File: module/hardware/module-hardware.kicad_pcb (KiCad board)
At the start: 4 copper layers, 45.7 x 102.9 mm, 75 parts, among them J1 USB_B_Micro, J10 Conn_01x03, J11 Conn_01x03, J12 Conn_01x03, J2 40Pin 0.1", J3 Conn_01x02_Male, J4 40Pin 0.1", J5 Conn_01x03_Male, J6 Conn_01x03_Male, J7 Conn_01x03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

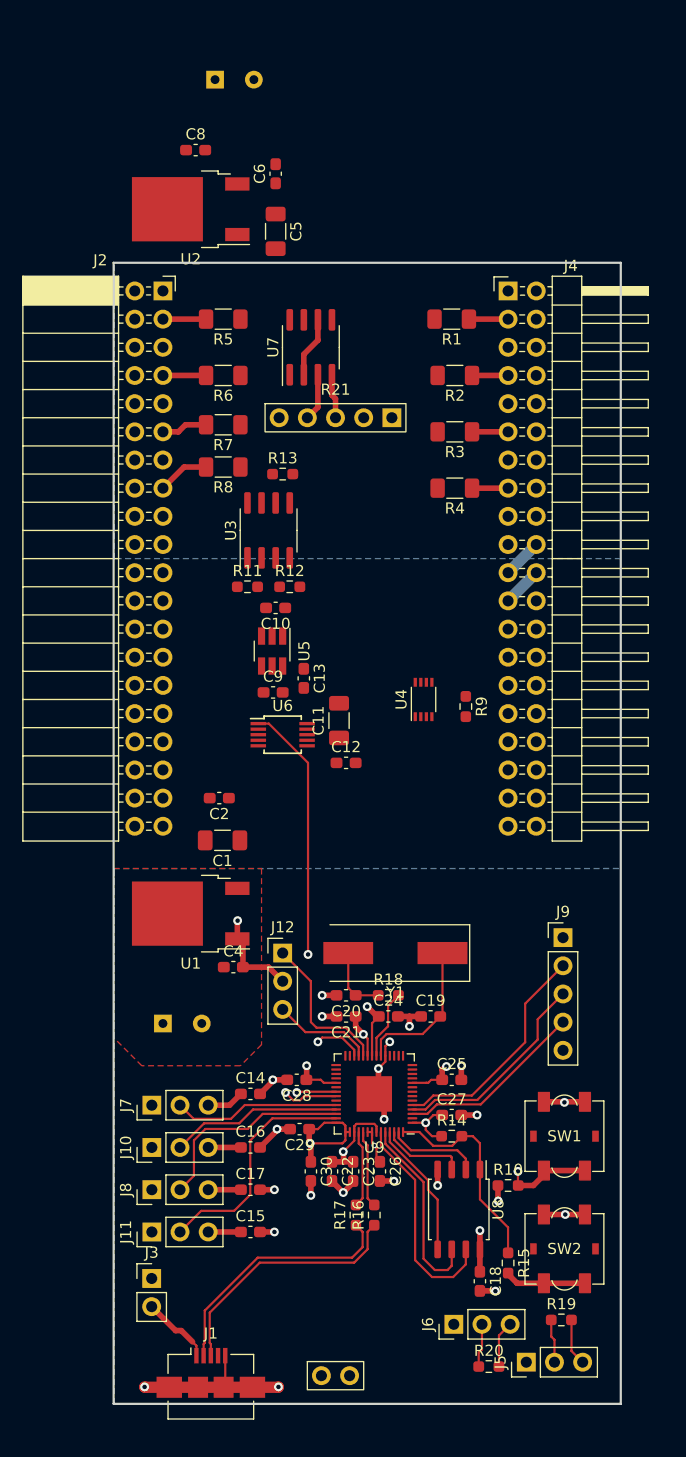
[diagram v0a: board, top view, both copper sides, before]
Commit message: Module Analog preliminaty routing complete
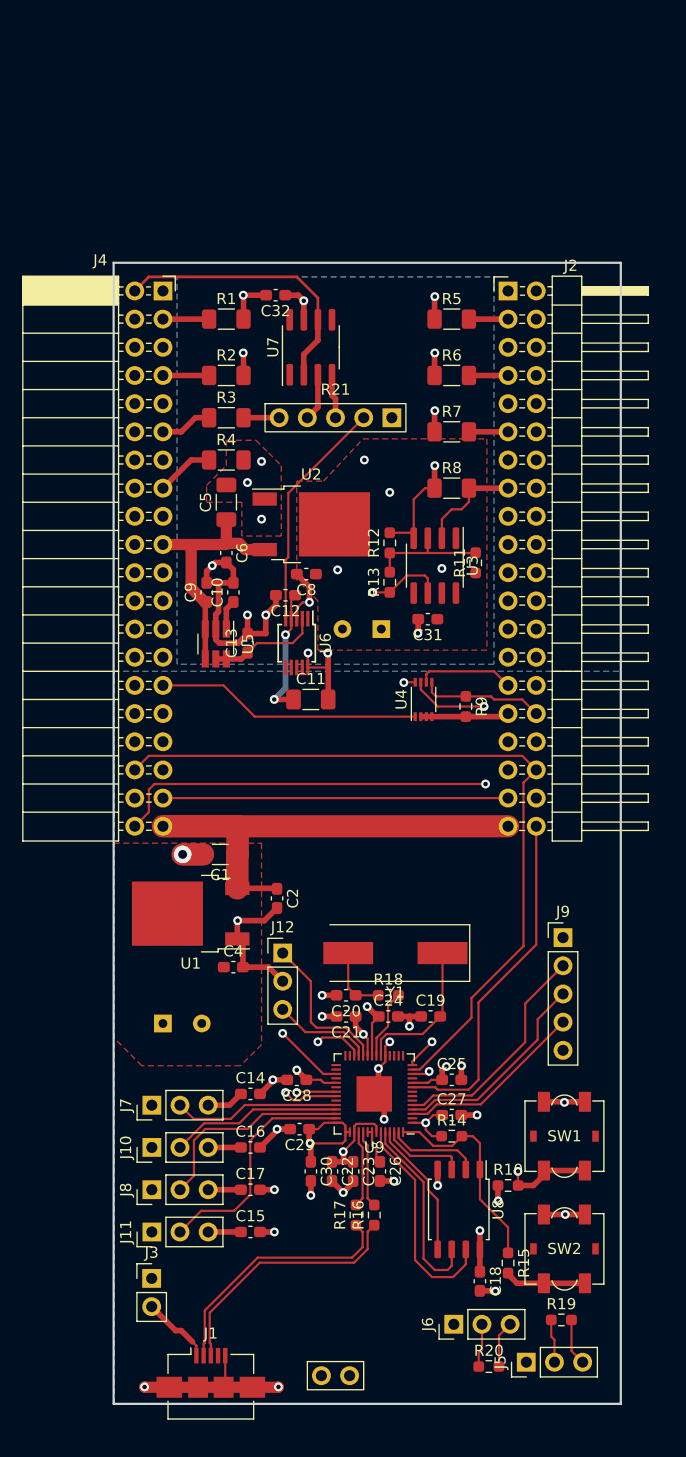
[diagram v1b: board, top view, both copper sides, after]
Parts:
- added C31: 0.1u, Capacitor_SMD:C_0603_1608Metric_Pad1.08x0.95mm_HandSolder, F.Cu at (151.5, 96.9)
- added C32: 0.1u, Capacitor_SMD:C_0603_1608Metric_Pad1.08x0.95mm_HandSolder, F.Cu at (137.8, 67.7)
- J2: footprint Connector_PinSocket_2.54mm:PinSocket_2x20_P2.54mm_Horizontal -> Connector_PinHeader_2.54mm:PinHeader_2x20_P2.54mm_Horizontal
- J4: footprint Connector_PinHeader_2.54mm:PinHeader_2x20_P2.54mm_Horizontal -> Connector_PinSocket_2.54mm:PinSocket_2x20_P2.54mm_Horizontal
- moved C7 51.7 mm to (147.3, 97.8), turned to 180 degrees
- moved C8 39.5 mm to (140.6, 92.8), turned to 180 degrees
- moved C6 34.5 mm to (133.3, 90.9), turned to -90 degrees
- moved J2 31.1 mm to (158.8, 67.3)
- moved J4 31.1 mm to (127.6, 67.3)
- moved U2 30.4 mm to (141.0, 88.4), turned to 0 degrees
- moved C5 24.8 mm to (133.3, 86.4), turned to 90 degrees
- moved R4 20.8 mm to (133.3, 82.5), turned to 0 degrees
- moved R8 20.7 mm to (153.7, 85.1), turned to 0 degrees
- moved R11 20.7 mm to (155.8, 91.8), turned to 90 degrees
- moved R3 20.6 mm to (133.3, 78.7), turned to 0 degrees
- moved R7 20.6 mm to (153.7, 80.0), turned to 0 degrees
- moved R2 20.6 mm to (133.3, 74.9), turned to 0 degrees
- moved R5 20.6 mm to (153.7, 69.8), turned to 0 degrees
- moved R6 20.6 mm to (153.7, 74.9), turned to 0 degrees
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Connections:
- C11 pad 2: GND -> GNDA
- C12 pad 2: GND -> GNDA
- U6 pad 4: (no net) -> +3V3
- U6 pad 7: +3V3 -> /DAC_LDACB
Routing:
- net /CBUS_EXTRA: track 0.00 -> 73.1 mm, vias 0 -> 1
- net /CBUS_SCK: track 0.00 -> 69.3 mm
- net GNDA: track 7.60 -> 74.5 mm, vias 0 -> 16
- net +5VA: track 0.00 -> 60.9 mm
- net /CBUS_DRDY: track 0.00 -> 60.3 mm, vias 0 -> 1
- net /CHANNEL_FULL: track 0.00 -> 57.9 mm, vias 0 -> 2
- net +5VD: track 0.00 -> 48.4 mm
- net /CBUS_SDOUT: track 0.00 -> 43.8 mm, vias 0 -> 2
- net /A7: track 3.25 -> 39.9 mm
- net /A5: track 3.25 -> 39.4 mm
- net /A3: track 3.25 -> 38.9 mm
- net /A1: track 3.53 -> 38.9 mm
- net /A2: track 3.89 -> 38.2 mm
- net /A4: track 3.89 -> 38.2 mm
- net /A6: track 4.15 -> 38.2 mm
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- added copper zone on B.Cu, net +3.3VA
- added copper zone on F.Cu, net +3.3VA
- added copper zone on In2.Cu, net +5VD
- added copper zone on F.Cu, net GNDA
- added copper zone on In1.Cu, net GNDA
- removed copper zone on B.Cu, net GNDA

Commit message: Finish Module PCB routing (DAC SPI lines)
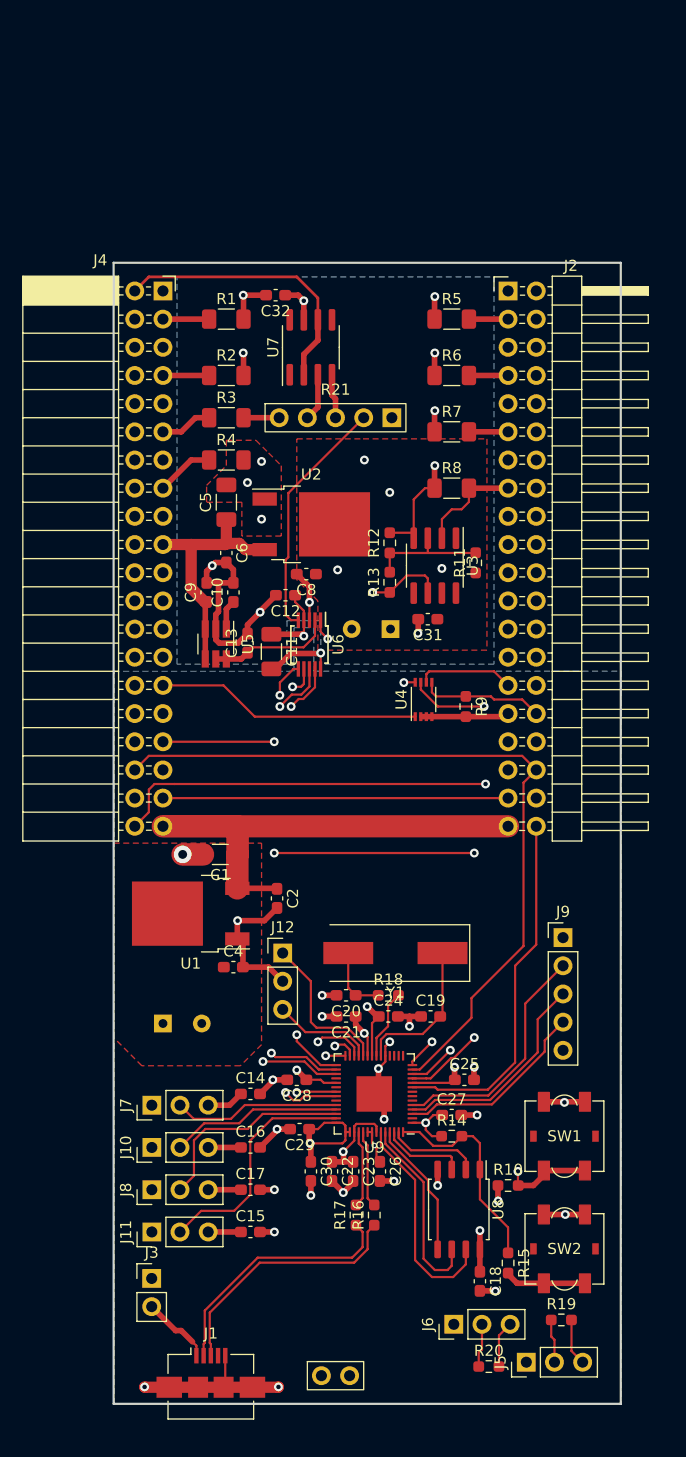
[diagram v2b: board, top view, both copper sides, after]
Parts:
- moved C11 5.59 mm to (137.4, 99.8), turned to -90 degrees
- moved U6 1.15 mm to (140.8, 99.2)
- moved C25 1.14 mm to (154.8, 138.4)
- moved C7 0.83 mm to (148.2, 97.8)
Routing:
- net /CBUS_SDIN: track 0.00 -> 61.8 mm, vias 0 -> 4
- net /DAC_SDAT: track 0.00 -> 43.3 mm, vias 0 -> 2
- net /RUN: track 41.8 -> 84.7 mm, vias 2 -> 3
- net /DAC_CSB: track 0.00 -> 39.9 mm, vias 0 -> 2
- net /DAC_SCK: track 0.00 -> 39.1 mm, vias 0 -> 2
- net /DAC_LDACB: track 0.00 -> 38.6 mm, vias 0 -> 2
- net /CHANNEL_FULL: track 57.9 -> 64.2 mm
- net GNDA: track 74.5 -> 70.3 mm, vias 16 -> 14
- net +3V3: track 72.8 -> 68.7 mm, vias 11 -> 10
- net Net-(C13-Pad1): track 10.1 -> 11.2 mm
- net /CBUS_EXTRA: track 73.1 -> 74.1 mm
- net Net-(R21-Pad2): track 21.0 -> 22.0 mm
- net /D.R.U.M. Module Digital/GPIO3_ENC2: track 20.8 -> 21.7 mm
- net /D.R.U.M. Module Digital/GPIO2_ENC1: track 19.0 -> 19.6 mm
- net /D.R.U.M. Module Digital/GPIO1_ENC0: track 17.0 -> 17.6 mm

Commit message: Fix +5V plane, cleanup silkscreen
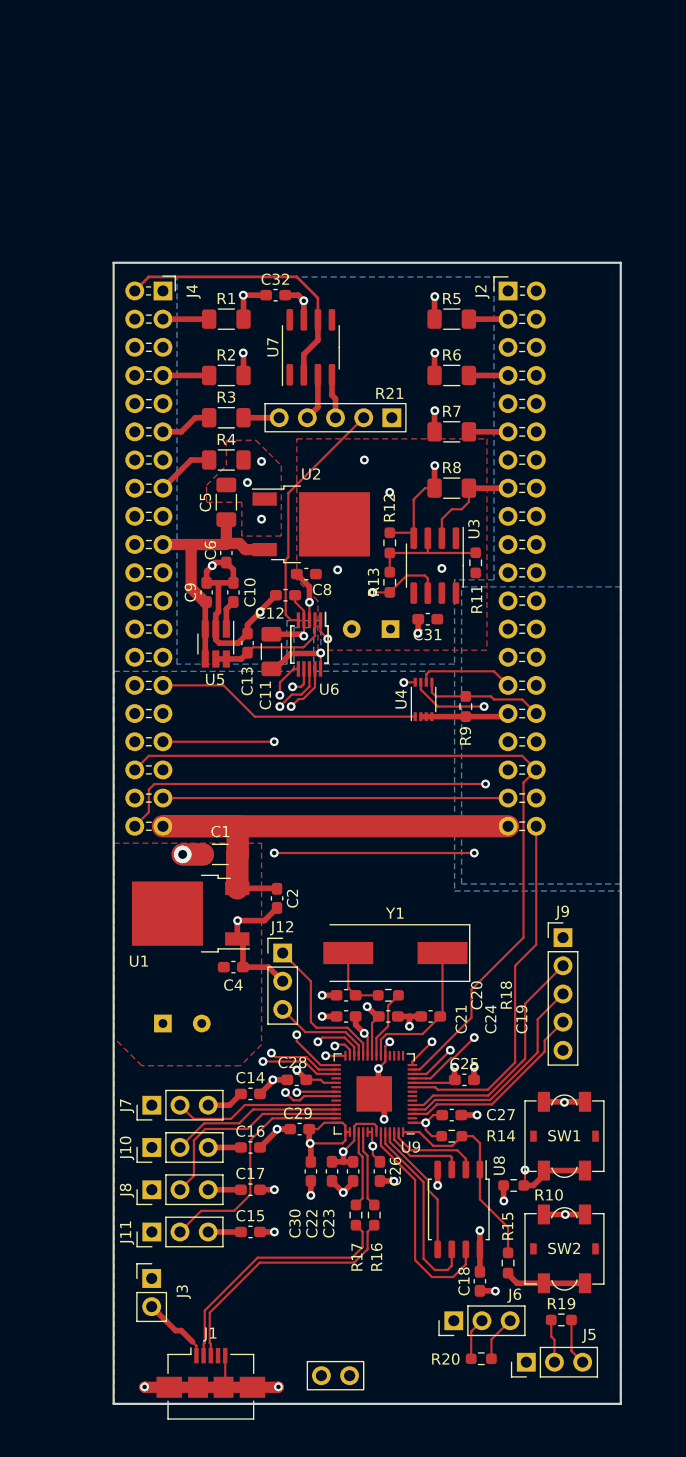
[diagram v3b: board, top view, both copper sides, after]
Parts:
- moved R20 0.98 mm to (156.3, 163.6)
- moved R10 0.51 mm to (159.3, 148.0)
- moved J6 0.32 mm to (153.9, 160.1)
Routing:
- added copper zone on B.Cu, net +5VD

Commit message: John Gibbons 30Khz LP & DAC analog power jumper
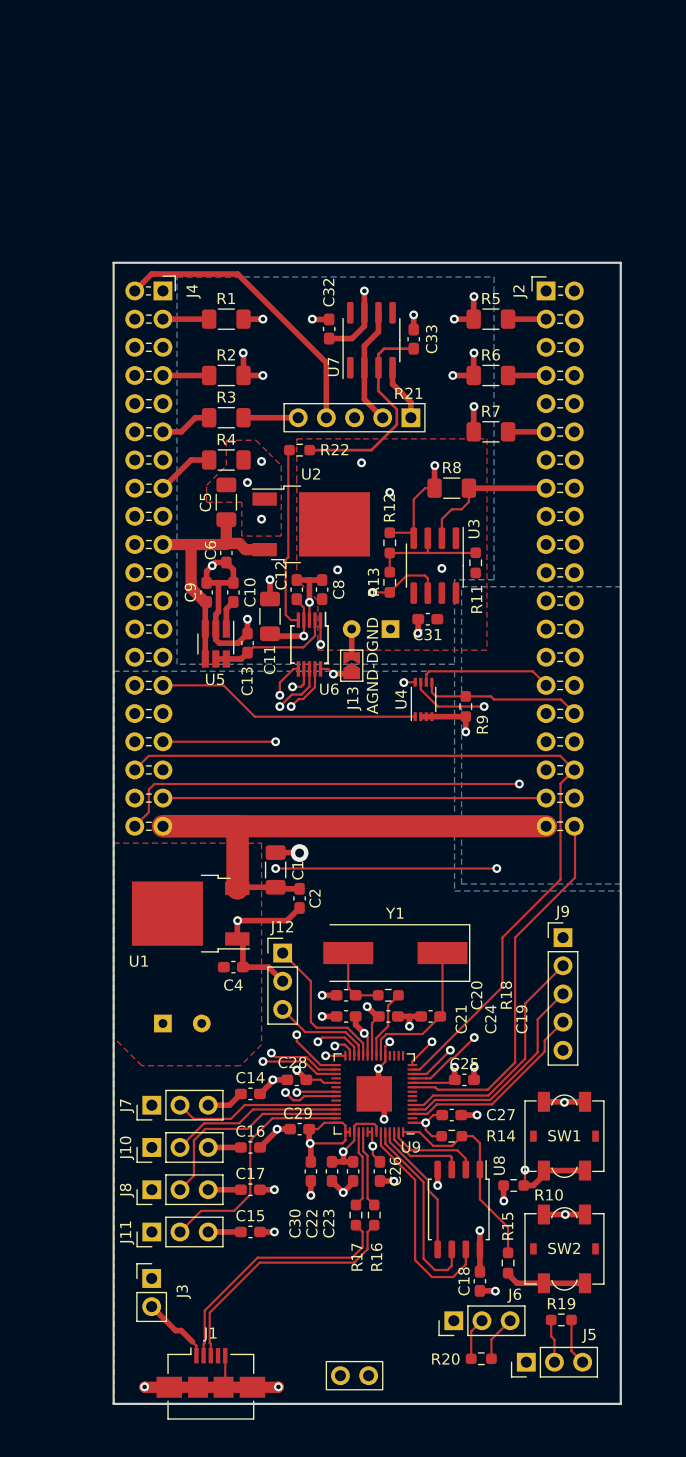
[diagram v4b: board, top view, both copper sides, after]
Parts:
- added C33: 510p, Capacitor_SMD:C_0603_1608Metric_Pad1.08x0.95mm_HandSolder, F.Cu at (150.2, 71.7)
- added J13: 0, Jumper:SolderJumper-2_P1.3mm_Open_TrianglePad1.0x1.5mm, F.Cu at (144.7, 101.1)
- added R22: 10k, Resistor_SMD:R_0603_1608Metric_Pad0.98x0.95mm_HandSolder, F.Cu at (140.0, 81.7)
- R21: value LINPOT-10KDB -> LINPOT-1KDB
- moved C32 5.71 mm to (142.6, 70.7), turned to 90 degrees
- moved U7 5.50 mm to (146.4, 71.8)
- moved C1 5.18 mm to (137.8, 119.5), turned to 90 degrees
- moved R5 3.53 mm to (157.2, 69.8)
- moved R6 3.53 mm to (157.2, 74.9)
- moved R7 3.53 mm to (157.2, 80.0)
- moved J2 3.43 mm to (162.2, 67.3)
- moved C11 3.18 mm to (137.3, 96.6), turned to 90 degrees
- moved C2 2.03 mm to (140.0, 122.1)
- moved C8 1.99 mm to (142.0, 94.2), turned to 90 degrees
- moved R21 1.71 mm to (144.9, 121.9)
- moved C12 1.14 mm to (139.7, 94.2), turned to 90 degrees
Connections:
- C11 pad 1: +3V3 -> +3.3VA
- C12 pad 1: +3V3 -> +3.3VA
- R21 pad 2: Net-(R21-Pad2) -> Net-(U7-Pad2)
- R21 pad 4: Net-(R21-Pad4) -> /Audio Out
- U6 pad 10: GNDA -> GND
- U6 pad 4: +3V3 -> +3.3VA
- U6 pad 5: Net-(R21-Pad2) -> Net-(U6-Pad5)
- U7 pad 2: /Audio Out -> Net-(U7-Pad2)
- U7 pad 3: Net-(R21-Pad4) -> Net-(U7-Pad3)
- U7 pad 6: /Audio Out -> Net-(U7-Pad2)
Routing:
- net Net-(R21-Pad2): track 22.0 -> 0.00 mm
- net Net-(U7-Pad3): track 0.00 -> 19.2 mm
- net Net-(U6-Pad5): track 0.00 -> 16.3 mm
- net Net-(U7-Pad2): track 0.00 -> 10.7 mm
- net +3.3VA: track 3.60 -> 13.4 mm, vias 5 -> 6
- net +3V3: track 68.6 -> 61.6 mm, vias 10 -> 9
- net +5VD: track 48.4 -> 54.0 mm
- net /CBUS_DRDY: track 60.3 -> 65.2 mm
- net /CBUS_EXTRA: track 74.1 -> 79.0 mm
- net GNDA: track 70.3 -> 75.2 mm, vias 14 -> 19
- net /CBUS_SCK: track 69.3 -> 74.1 mm
- net /A6: track 38.2 -> 42.8 mm
- net /A7: track 39.9 -> 44.4 mm
- net /CBUS_SDOUT: track 43.8 -> 48.1 mm
- net Net-(R21-Pad4): track 4.27 -> 0.00 mm
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- added copper zone on In2.Cu, net GNDA
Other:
- board text added: "AGND-DGND"

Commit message: Add pull down button resistor option
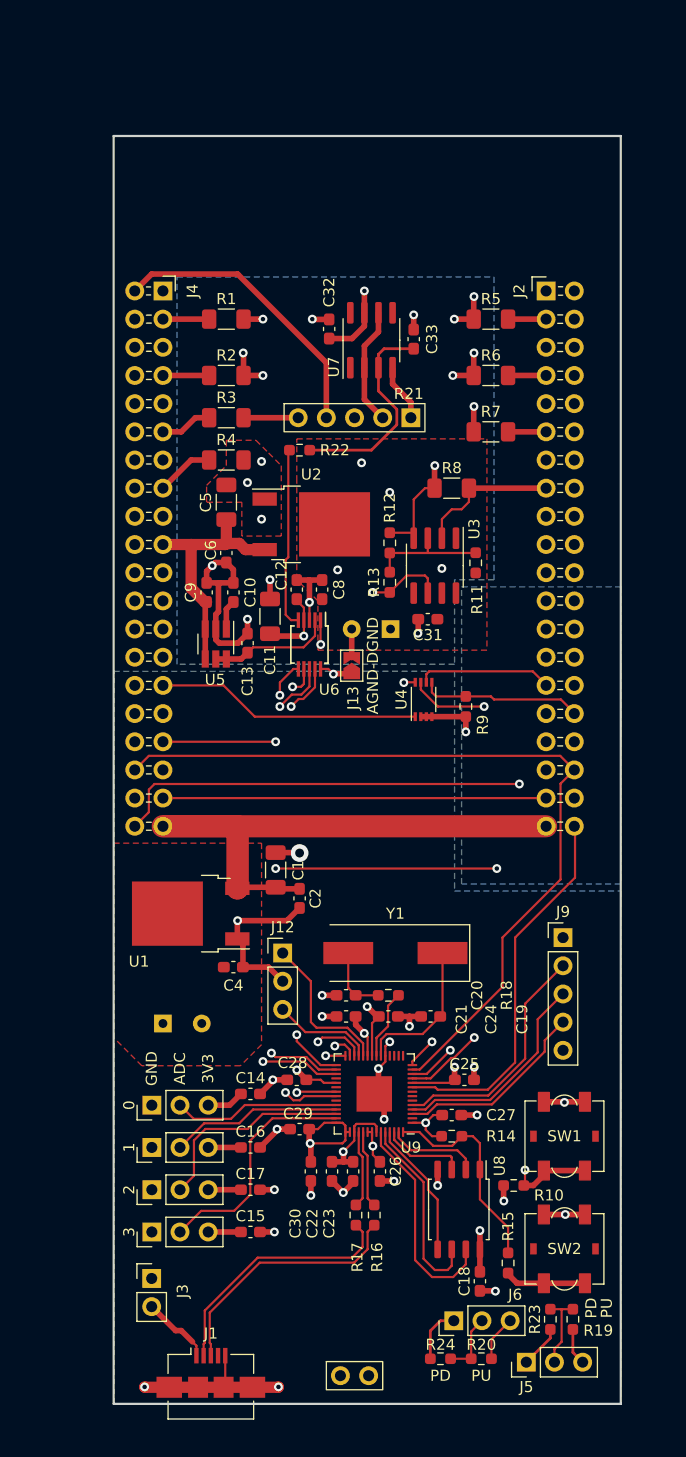
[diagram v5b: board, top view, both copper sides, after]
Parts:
- added R23: 10k, Resistor_SMD:R_0603_1608Metric_Pad0.98x0.95mm_HandSolder, F.Cu at (162.6, 160.0)
- added R24: 10k, Resistor_SMD:R_0603_1608Metric_Pad0.98x0.95mm_HandSolder, F.Cu at (152.7, 163.6)
- moved R19 1.04 mm to (164.6, 160.0), turned to -90 degrees
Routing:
- net GND: track 88.2 -> 97.1 mm
- net /D.R.U.M. Module Digital/GPIO4_BTN0: track 48.1 -> 51.3 mm
- net /D.R.U.M. Module Digital/GPIO5_BTN1: track 41.4 -> 43.3 mm
- net +3V3: track 61.6 -> 60.7 mm
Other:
- board size 45.7 x 102.9 mm -> 45.7 x 114.3 mm
- board text added: "0"
- board text added: "1"
- board text added: "2"
- board text added: "3"
- board text added: "3V3"
- board text added: "ADC"
- board text added: "GND"
- board text added: "PD"
- board text added: "PU"

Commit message: Add M3 mounting holes; add HW/Layout REV IDs
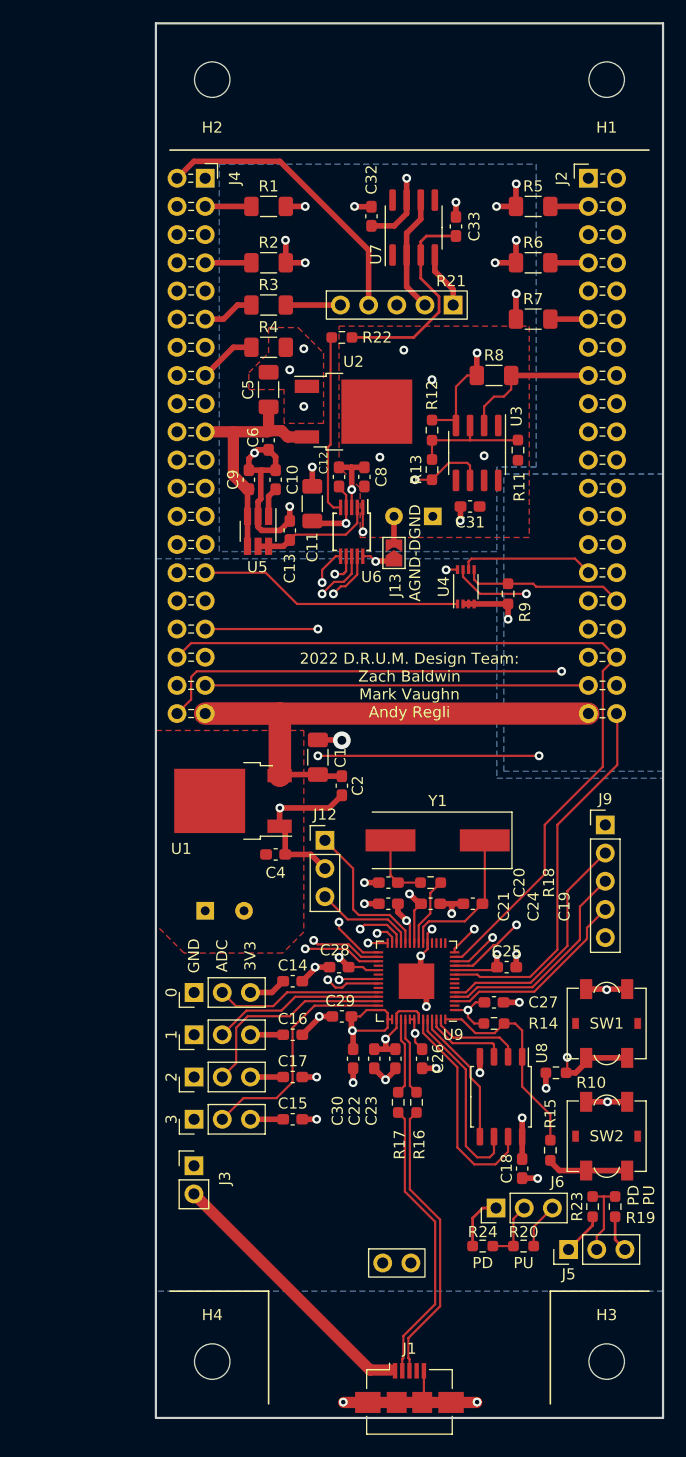
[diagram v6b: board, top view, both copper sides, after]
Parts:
- added H1: MountingHole, MountingHole:MountingHole_3.2mm_M3, F.Cu at (167.6, 48.3)
- added H2: MountingHole, MountingHole:MountingHole_3.2mm_M3, F.Cu at (132.1, 48.3)
- added H3: MountingHole, MountingHole:MountingHole_3.2mm_M3, F.Cu at (167.6, 163.8)
- added H4: MountingHole, MountingHole:MountingHole_3.2mm_M3, F.Cu at (132.1, 163.8)
- moved J1 18.0 mm to (149.9, 166.2)
- moved C17 10.9 mm to (139.3, 138.2)
- moved R10 10.9 mm to (163.1, 137.8)
- moved R16 10.9 mm to (150.5, 140.5)
- moved R17 10.9 mm to (148.8, 140.5)
- moved J8 10.9 mm to (130.4, 138.2)
- moved C1 10.9 mm to (141.6, 109.3)
- moved C11 10.9 mm to (141.1, 86.5)
- moved C7 10.9 mm to (152.0, 87.6)
- moved J9 10.9 mm to (167.5, 115.4)
- moved R13 10.9 mm to (151.9, 83.4)
- moved R2 10.9 mm to (137.2, 64.8)
- moved R6 10.9 mm to (161.0, 64.8)
- moved R7 10.9 mm to (161.0, 69.8)
- moved R9 10.9 mm to (158.8, 94.6)
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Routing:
- net Net-(J1-Pad1): track 6.39 -> 24.4 mm
- net /USB_D-: track 22.9 -> 25.9 mm
- net /USB_D+: track 22.9 -> 25.9 mm
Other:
- board size 45.7 x 114.3 mm -> 45.7 x 125.7 mm
- board text added: "2022 D.R.U.M. Design Team: Zach Baldwin Mark Vaughn Andy Regli"
- board text added: "D.R.U.M. - Module HW Design REV: 1.0 Layout REV: A Order No. P/N DRUM-DM-1000"
